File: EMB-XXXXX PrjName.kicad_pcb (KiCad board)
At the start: 4 copper layers, 110 x 60 mm, 12 parts

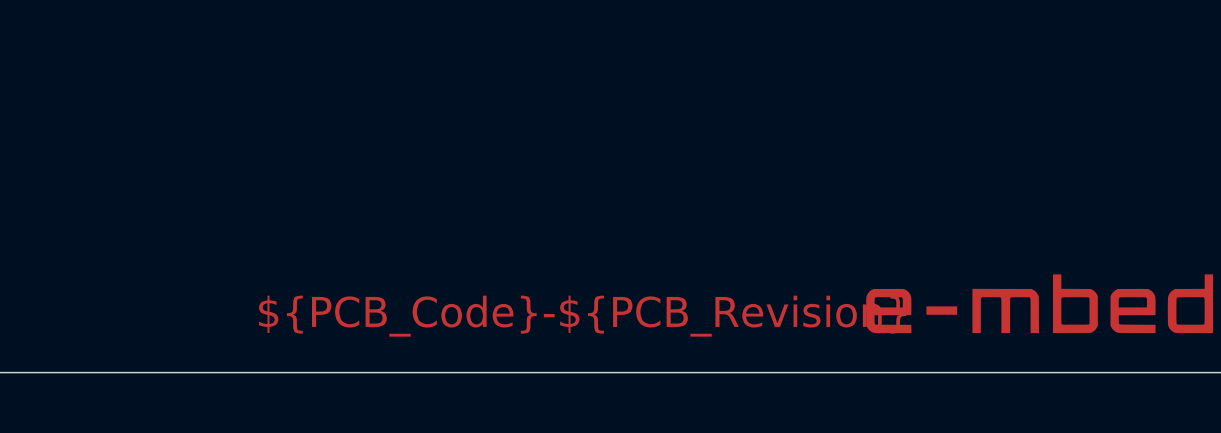
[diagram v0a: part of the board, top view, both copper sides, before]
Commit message: Local library added
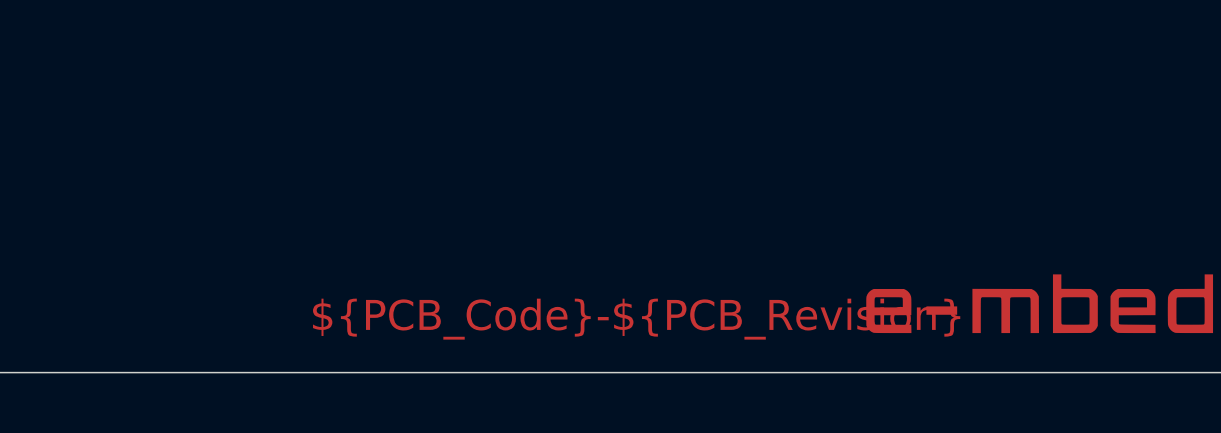
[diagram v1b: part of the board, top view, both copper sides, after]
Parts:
- moved Co1 1.80 mm to (145.8, 135.8)
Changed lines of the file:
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@@
 		)
 		(property "Value" "MountingHole"
-			(at 0 3.75 0)
+			(at -8.4 0 0)
 			(layer "F.Fab")
 			(effects
@@
 			(solder_mask_margin 0.5)
 			(clearance 0.5)
-		)
-	)
-	(footprint "e-mbedLocalLib:PCBCodeCopper"
-		(layer "F.Cu")
-		(at 143.985786 135.685786)
-		(property "Reference" "Co1"
-			(at 0 -0.5 0)
-			(unlocked yes)
-			(layer "F.SilkS")
-			(hide yes)
-			(effects
-				(font
-					(size 1 1)
-					(thickness 0.1)
-				)
-			)
-		)
-		(property "Value" "~"
-			(at 0 1 0)
-			(unlocked yes)
-			(layer "F.Fab")
-			(effects
-				(font
-					(size 1 1)
-					(thickness 0.15)
-				)
-			)
-		)
-		(property "Footprint" "e-mbedLocalLib:PCBCodeCopper"
-			(at 0 0 0)
-			(unlocked yes)
-			(layer "F.Fab")
-			(hide yes)
-			(effects
-				(font
-					(size 1 1)
-					(thickness 0.15)
-				)
-			)
-		)
-		(property "Datasheet" ""
-			(at 0 0 0)
-			(unlocked yes)
-			(layer "F.Fab")
-			(hide yes)
-			(effects
-				(font
-					(size 1 1)
-					(thickness 0.15)
-				)
-			)
-		)
-		(property "Description" ""
-			(at 0 0 0)
-			(unlocked yes)
-			(layer "F.Fab")
-			(hide yes)
-			(effects
-				(font
-					(size 1 1)
-					(thickness 0.15)
-				)
-			)
-		)
-		(sheetname "Miscellaneous")
-		(sheetfile "Miscellaneous.kicad_sch")
-		(attr smd exclude_from_bom)
-		(fp_text user "${PCB_Code}-${PCB_Revision}"
-			(at 0 0.5 0)
-			(unlocked yes)
-			(layer "F.Cu")
-			(effects
-				(font
-					(size 1 1)
-					(thickness 0.15)
-				)
-				(justify bottom)
-			)
-		)
-		(fp_text user "${REFERENCE}"
-			(at 0 2.5 0)
-			(unlocked yes)
-			(layer "F.Fab")
-			(effects
-				(font
-					(size 1 1)
-					(thickness 0.15)
-				)
-			)
 		)
 	)
@@
 		)
 	)
+	(footprint "e-mbedLocalLib:PCBCodeCopper"
+		(layer "F.Cu")
+		(at 145.785786 135.785786)
+		(property "Reference" "Co1"
+			(at 0 -0.5 0)
+			(unlocked yes)
+			(layer "F.SilkS")
+			(hide yes)
+			(effects
+				(font
+					(size 1 1)
+					(thickness 0.1)
+				)
+			)
+		)
+		(property "Value" "~"
+			(at 0 1 0)
+			(unlocked yes)
+			(layer "F.Fab")
+			(effects
+				(font
+					(size 1 1)
+					(thickness 0.15)
+				)
+			)
+		)
+		(property "Footprint" "e-mbedLocalLib:PCBCodeCopper"
+			(at 0 0 0)
+			(unlocked yes)
+			(layer "F.Fab")
+			(hide yes)
+			(effects
+				(font
+					(size 1 1)
+					(thickness 0.15)
+				)
+			)
+		)
+		(property "Datasheet" ""
+			(at 0 0 0)
+			(unlocked yes)
+			(layer "F.Fab")
+			(hide yes)
+			(effects
+				(font
+					(size 1 1)
+					(thickness 0.15)
+				)
+			)
+		)
+		(property "Description" ""
+			(at 0 0 0)
+			(unlocked yes)
+			(layer "F.Fab")
+			(hide yes)
+			(effects
+				(font
+					(size 1 1)
+					(thickness 0.15)
+				)
+			)
+		)
+		(sheetname "Miscellaneous")
+		(sheetfile "Miscellaneous.kicad_sch")
+		(attr smd exclude_from_bom)
+		(fp_text user "${PCB_Code}-${PCB_Revision}"
+			(at 0 0.5 0)
+			(unlocked yes)
+			(layer "F.Cu")
+			(effects
+				(font
+					(size 1 1)
+					(thickness 0.15)
+				)
+				(justify bottom)
+			)
+		)
+		(fp_text user "${REFERENCE}"
+			(at 0 2.5 0)
+			(unlocked yes)
+			(layer "F.Fab")
+			(effects
+				(font
+					(size 1 1)
+					(thickness 0.15)
+				)
+			)
+		)
+	)
